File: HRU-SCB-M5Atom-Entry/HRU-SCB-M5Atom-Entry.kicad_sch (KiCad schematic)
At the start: 11 parts, among them J1 GROVE-CONNECTOR-DIP_4P-2.0_

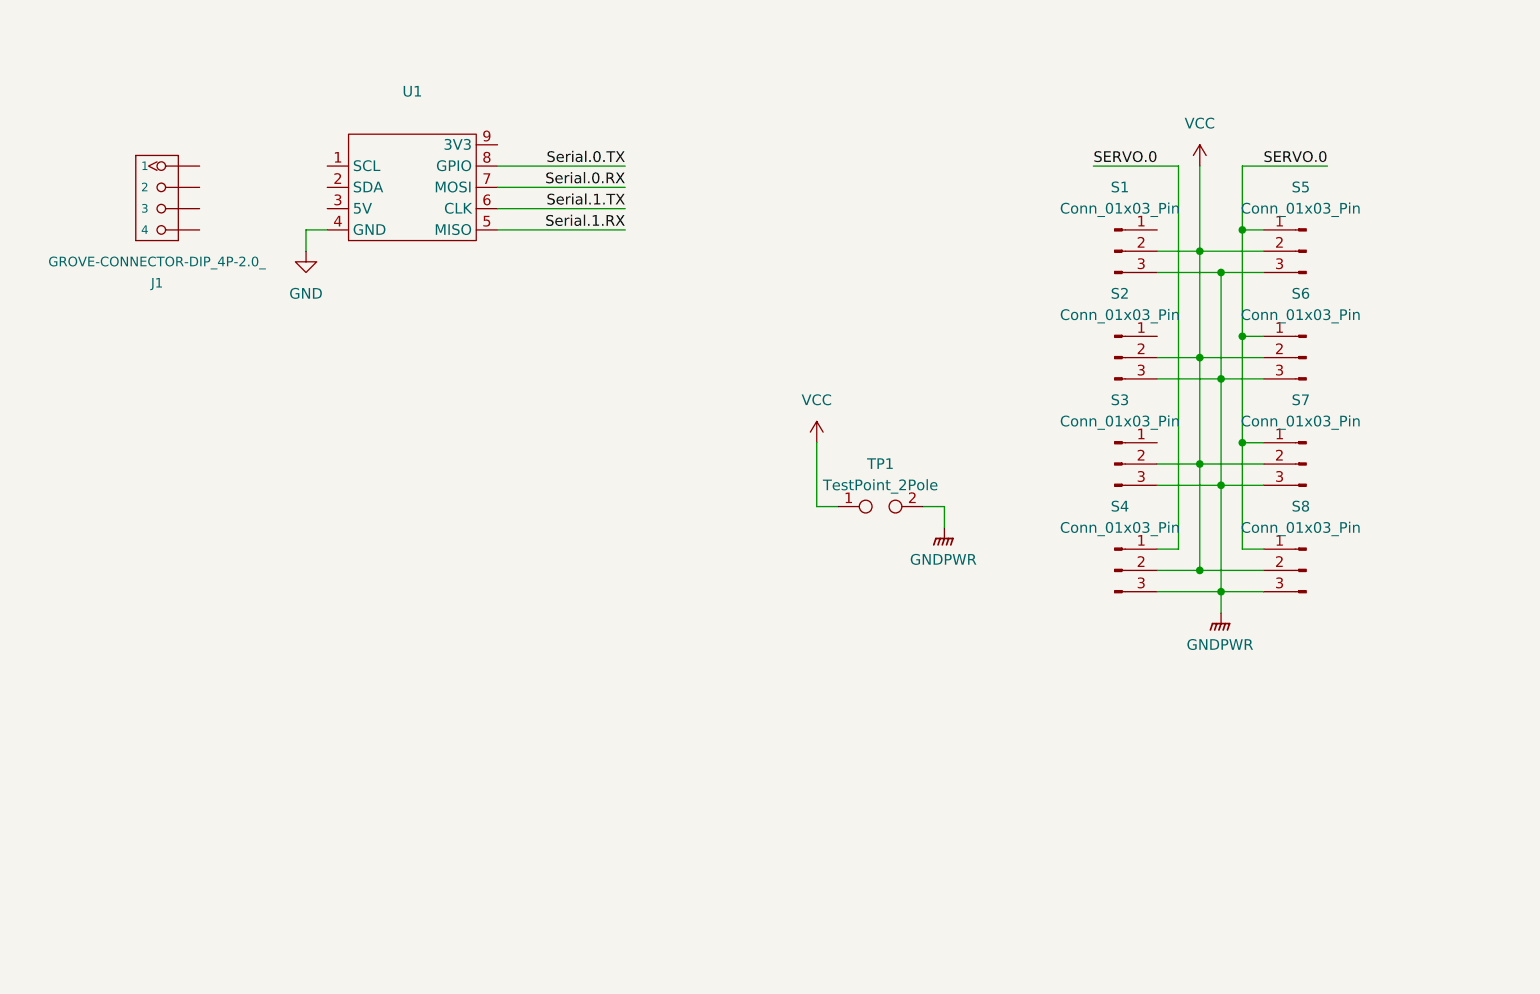
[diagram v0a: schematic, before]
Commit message: Update: M5Atom entry board with Grove port
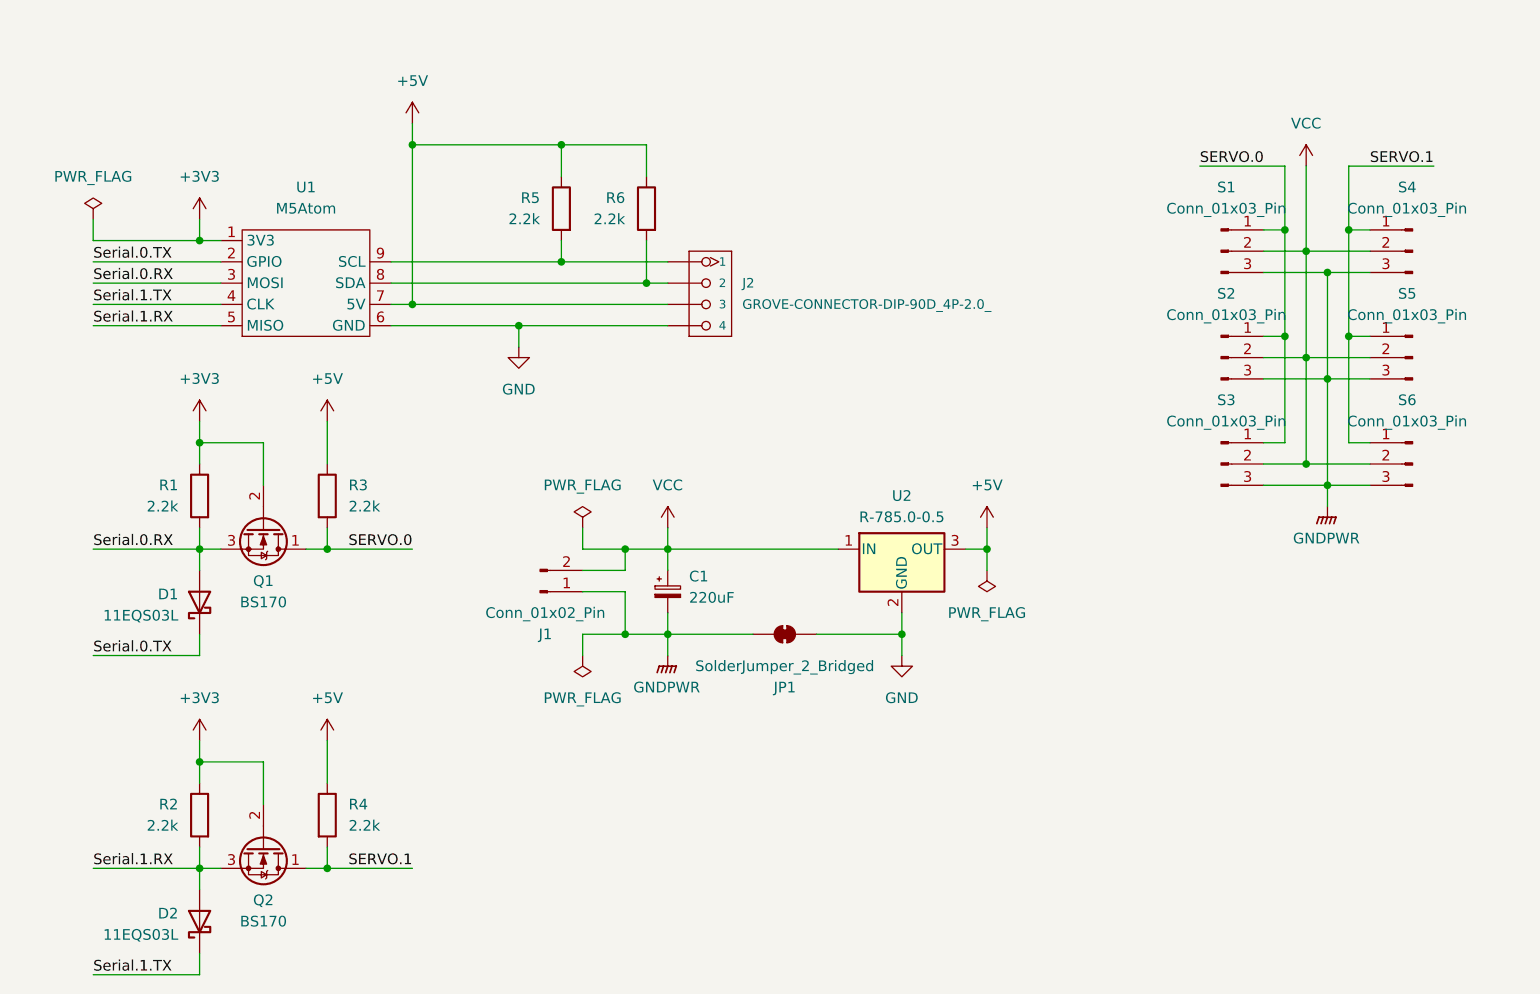
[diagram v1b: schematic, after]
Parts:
- removed J1: GROVE-CONNECTOR-DIP_4P-2.0_, OPL_Connector:GROVE-HW4-2.0, symbol OPL_Connector:GROVE-CONNECTOR-DIP_4P-2.0_
- removed S4, S7, S8: Conn_01x03_Pin, Connector_PinHeader_2.54mm:PinHeader_1x03_P2.54mm_Vertical, symbol Connector:Conn_01x03_Pin
- removed TP1: TestPoint_2Pole, TestPoint:TestPoint_2Pads_Pitch5.08mm_Drill1.3mm, symbol Connector:TestPoint_2Pole
- added C1: 220uF, Capacitor_THT:CP_Radial_D6.3mm_P2.50mm, symbol Device:C_Polarized_Small
- added D1, D2: 11EQS03L, Diode_THT:D_T-1_P5.08mm_Horizontal, symbol Device:D_Schottky
- added J1: Conn_01x02_Pin, Connector_AMASS:AMASS_XT30U-M_1x02_P5.0mm_Vertical, symbol Connector:Conn_01x02_Pin
- added J2: GROVE-CONNECTOR-DIP-90D_4P-2.0_, OPL_Connector:GROVE-HW4-2.0-90D, symbol OPL_Connector:GROVE-CONNECTOR-DIP-90D_4P-2.0_
- added JP1: SolderJumper_2_Bridged, Jumper:SolderJumper-2_P1.3mm_Bridged_Pad1.0x1.5mm, symbol Jumper:SolderJumper_2_Bridged
- added Q1, Q2: BS170, Package_TO_SOT_THT:TO-92_Inline, symbol Transistor_FET:BS170
- added R1, R2, R3, R4, R5, R6: 2.2k, Resistor_THT:R_Axial_DIN0207_L6.3mm_D2.5mm_P7.62mm_Horizontal, symbol Device:R
- added S6: Conn_01x03_Pin, Connector_PinHeader_2.54mm:PinHeader_1x03_P2.54mm_Vertical, symbol Connector:Conn_01x03_Pin
- added U2: R-785.0-0.5, Converter_DCDC:Converter_DCDC_RECOM_R-78E-0.5_THT, symbol Regulator_Switching:R-785.0-0.5
- U1: value ~ -> M5Atom
- renumbered S5 to S4, S6 to S5
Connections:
- net GND: now also U1.6 (GND), J2.4, JP1.2 (B), U2.2 (GND); no longer U1.4 (GND)
- net GNDPWR: now also C1.2, J1.1 (Pin_1), JP1.1 (A), S6.3 (Pin_3)
- net SERVO.0: now also S1.1 (Pin_1), S2.1 (Pin_1), S3.1 (Pin_1), Q1.1 (D), R3.2; no longer S4.1 (Pin_1), S5.1 (Pin_1)
- net Serial.0.RX: now also U1.3 (MOSI), D1.2 (A), Q1.3 (S), R1.2; no longer U1.7 (MOSI)
- net Serial.0.TX: now also U1.2 (GPIO), D1.1 (K); no longer U1.8 (GPIO)
- net Serial.1.RX: now also D2.2 (A), Q2.3 (S), R2.2
- net Serial.1.TX: now also U1.4 (CLK), D2.1 (K); no longer U1.6 (CLK)
- net VCC: now also C1.1, J1.2 (Pin_2), S6.2 (Pin_2), U2.1 (IN)
- net +3V3: now reaches U1.1 (3V3)
- net +3V3: now also Q1.2 (G), Q2.2 (G), R1.1, R2.1
- net at U1.9 (SCL): now also J2.1, R5.2
- new net: J2.2, R6.2, U1.8 (SDA)
- new net +5V: J2.3, R3.1, R4.1, R5.1, R6.1, U1.7 (5V), U2.3 (OUT)
- new net SERVO.1: Q2.1 (D), R4.2, S4.1 (Pin_1), S5.1 (Pin_1), S6.1 (Pin_1)
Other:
- moved on the sheet: S1, S2, S4, S5

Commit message: Update: parts layout and smaller board
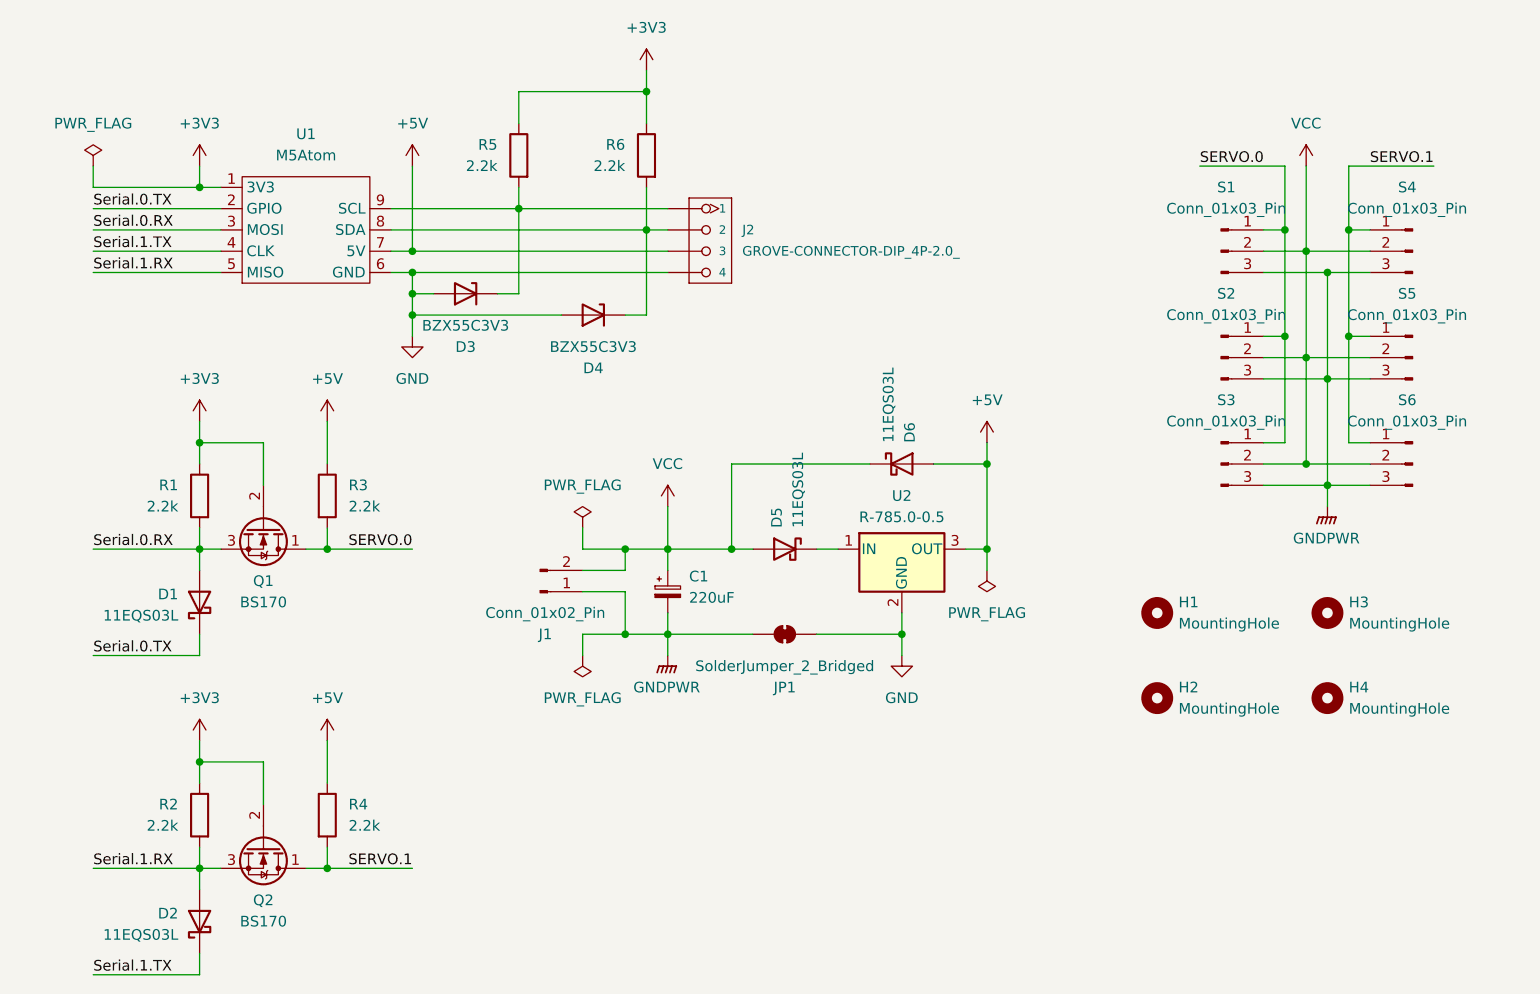
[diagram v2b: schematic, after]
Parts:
- removed J2: GROVE-CONNECTOR-DIP-90D_4P-2.0_, OPL_Connector:GROVE-HW4-2.0-90D, symbol OPL_Connector:GROVE-CONNECTOR-DIP-90D_4P-2.0_
- added D3, D4: BZX55C3V3, Diode_THT:D_T-1_P5.08mm_Horizontal, symbol Device:D_Zener
- added D5, D6: 11EQS03L, Diode_THT:D_T-1_P5.08mm_Horizontal, symbol Device:D_Schottky
- added H1, H2, H3, H4: MountingHole, MountingHole:MountingHole_2.2mm_M2, symbol Mechanical:MountingHole
- added J2: GROVE-CONNECTOR-DIP_4P-2.0_, OPL_Connector:GROVE-HW4-2.0, symbol OPL_Connector:GROVE-CONNECTOR-DIP_4P-2.0_
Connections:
- net +3V3: now also R5.1, R6.1
- net +5V: now also D6.2 (A), J2.3; no longer R5.1, R6.1
- net GND: now also D3.2 (A), D4.2 (A), J2.4
- net VCC: now also D5.2 (A), D6.1 (K); no longer U2.1 (IN)
- net at R6.2, U1.8 (SDA): now also D4.1 (K), J2.2
- net at R5.2, U1.9 (SCL): now also D3.1 (K), J2.1
- new net: D5.1 (K), U2.1 (IN)
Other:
- moved on the sheet: R5, R6, U1

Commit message: update: non-via circuit
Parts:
- S1, S2, S3, S4, S5, S6: footprint Connector_PinHeader_2.54mm:PinHeader_1x03_P2.54mm_Vertical -> mymod:PinHeader_1x03_P2.54mm_Vertical_SmallCourtyard
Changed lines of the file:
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@@
 			)
 		)
-		(property "Footprint" "Connector_PinHeader_2.54mm:PinHeader_1x03_P2.54mm_Vertical"
+		(property "Footprint" "mymod:PinHeader_1x03_P2.54mm_Vertical_SmallCourtyard"
 			(at 182.88 66.04 0)
 			(effects
@@
 			)
 		)
-		(property "Footprint" "Connector_PinHeader_2.54mm:PinHeader_1x03_P2.54mm_Vertical"
+		(property "Footprint" "mymod:PinHeader_1x03_P2.54mm_Vertical_SmallCourtyard"
 			(at 182.88 40.64 0)
 			(effects
@@
 			)
 		)
-		(property "Footprint" "Connector_PinHeader_2.54mm:PinHeader_1x03_P2.54mm_Vertical"
+		(property "Footprint" "mymod:PinHeader_1x03_P2.54mm_Vertical_SmallCourtyard"
 			(at 160.02 66.04 0)
 			(effects
@@
 			)
 		)
-		(property "Footprint" "Connector_PinHeader_2.54mm:PinHeader_1x03_P2.54mm_Vertical"
+		(property "Footprint" "mymod:PinHeader_1x03_P2.54mm_Vertical_SmallCourtyard"
 			(at 160.02 53.34 0)
 			(effects
@@
 			)
 		)
-		(property "Footprint" "Connector_PinHeader_2.54mm:PinHeader_1x03_P2.54mm_Vertical"
+		(property "Footprint" "mymod:PinHeader_1x03_P2.54mm_Vertical_SmallCourtyard"
 			(at 182.88 53.34 0)
 			(effects
@@
 			)
 		)
-		(property "Footprint" "Connector_PinHeader_2.54mm:PinHeader_1x03_P2.54mm_Vertical"
+		(property "Footprint" "mymod:PinHeader_1x03_P2.54mm_Vertical_SmallCourtyard"
 			(at 160.02 40.64 0)
 			(effects

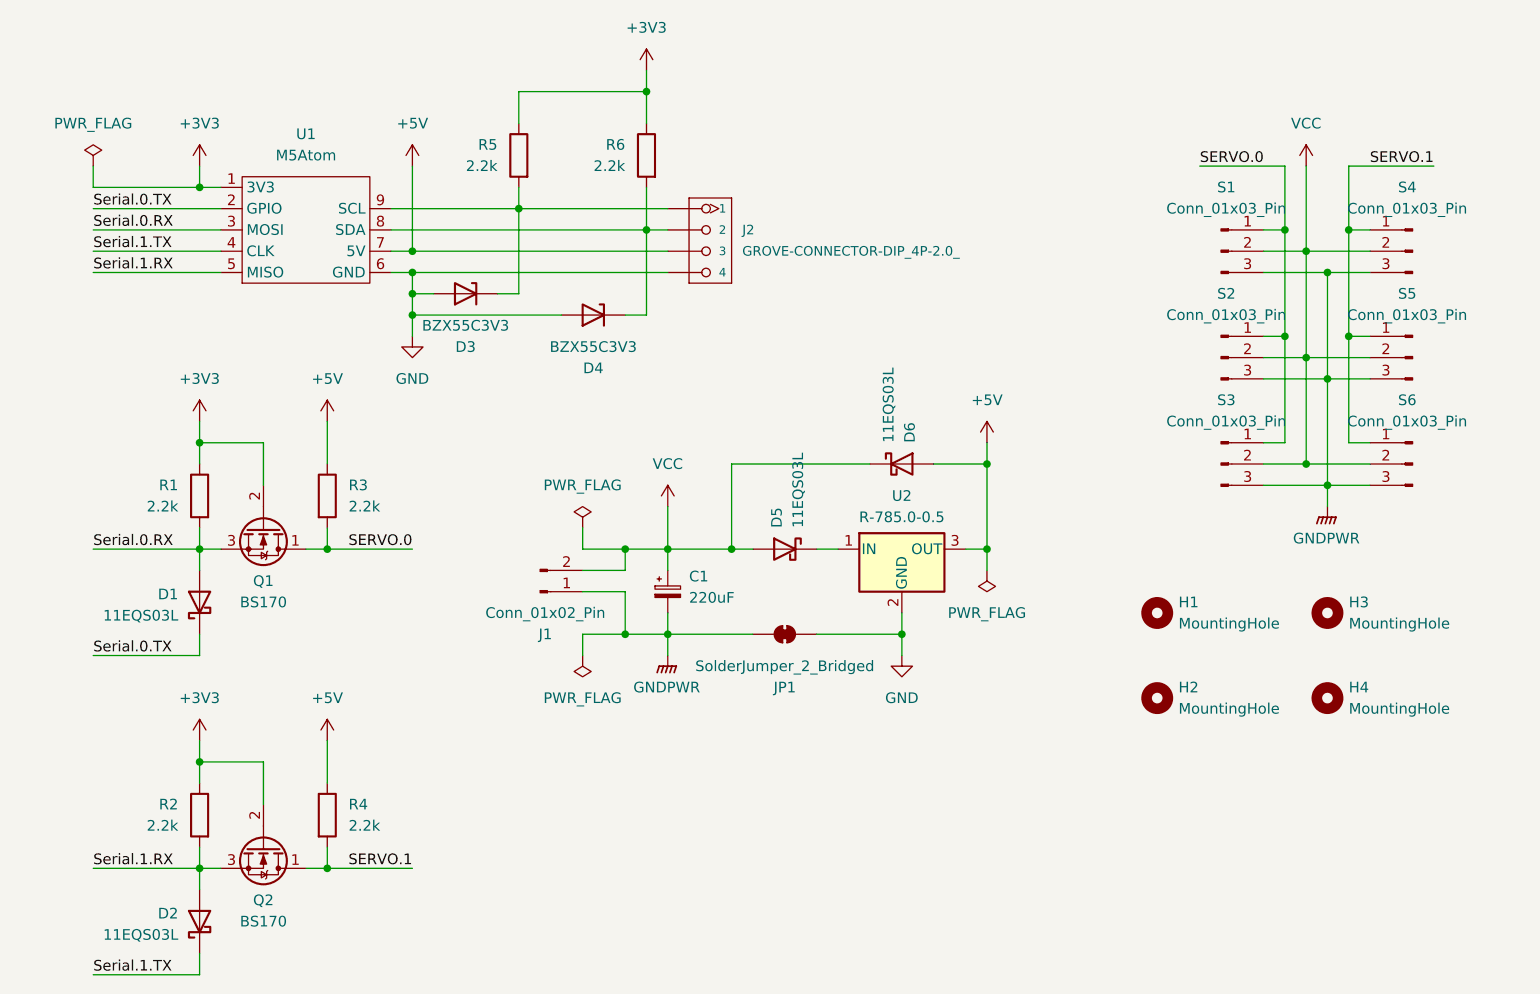
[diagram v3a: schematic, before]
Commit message: update: larger board outline for flesh members
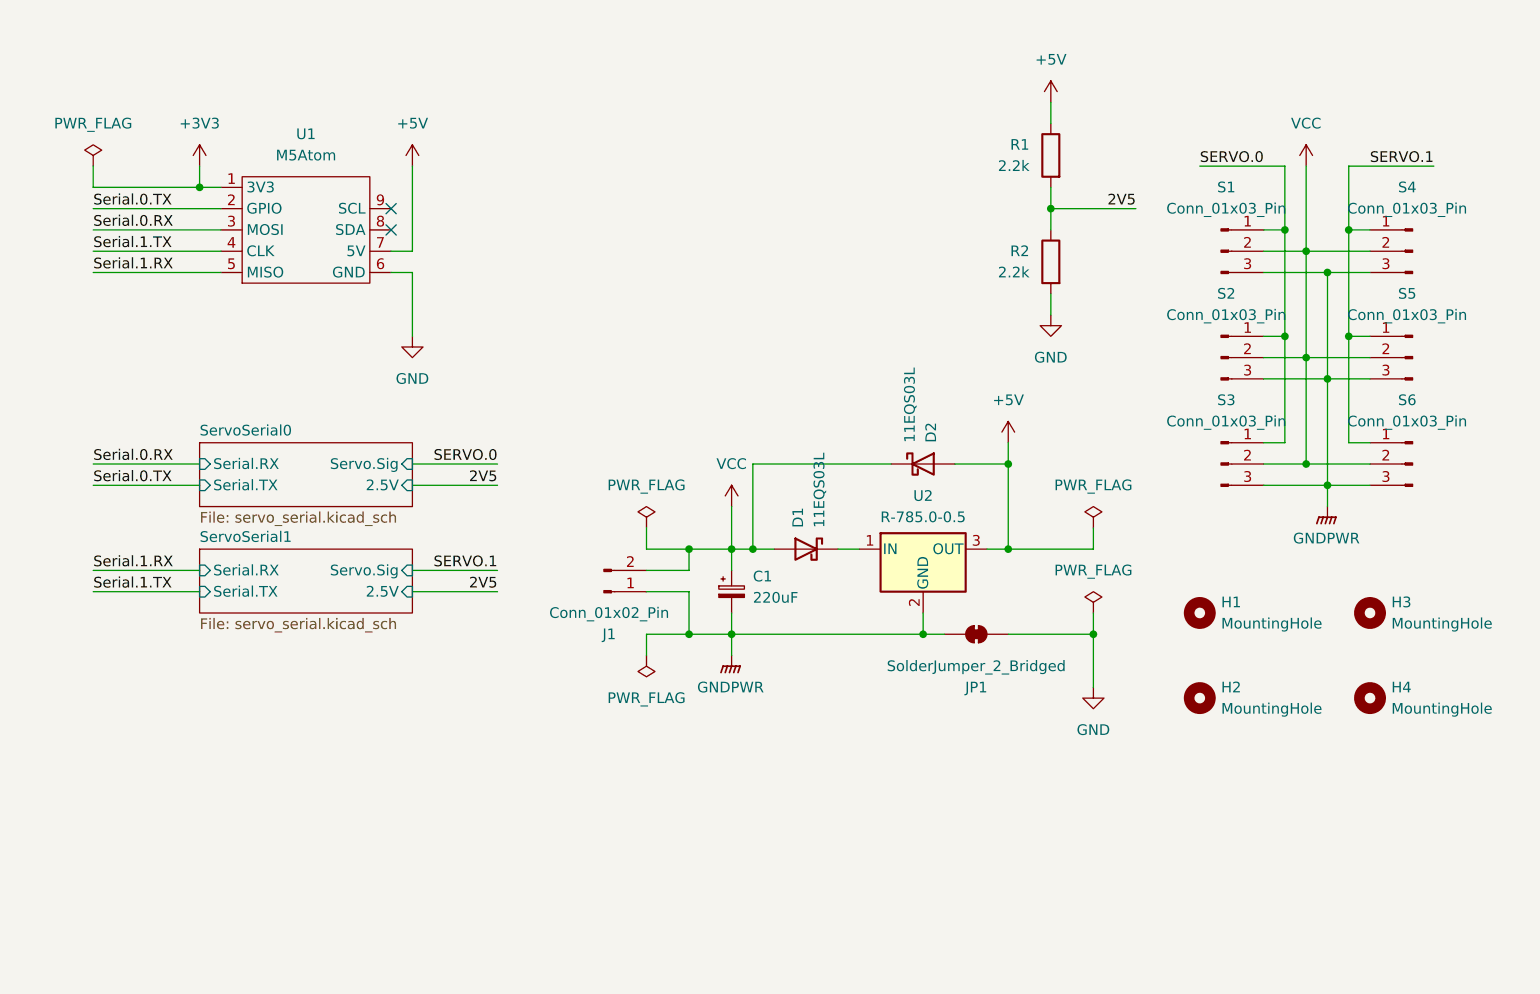
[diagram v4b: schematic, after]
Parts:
- removed D1, D2: 11EQS03L, Diode_THT:D_T-1_P5.08mm_Horizontal, symbol Device:D_Schottky
- removed D3, D4: BZX55C3V3, Diode_THT:D_T-1_P5.08mm_Horizontal, symbol Device:D_Zener
- removed J2: GROVE-CONNECTOR-DIP_4P-2.0_, OPL_Connector:GROVE-HW4-2.0, symbol OPL_Connector:GROVE-CONNECTOR-DIP_4P-2.0_
- removed Q1, Q2: BS170, Package_TO_SOT_THT:TO-92_Inline, symbol Transistor_FET:BS170
- removed R3, R4, R5, R6: 2.2k, Resistor_THT:R_Axial_DIN0207_L6.3mm_D2.5mm_P7.62mm_Horizontal, symbol Device:R
- renumbered D5 to D1, D6 to D2
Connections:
- net +3V3: no longer R1.1, R2.1
- net +5V: now also R1.1
- net GND: now also R2.2; no longer U2.2 (GND)
- net GNDPWR: now also U2.2 (GND)
- net Serial.0.RX: no longer R1.2
- net Serial.1.RX: no longer R2.2
- new net 2V5: R1.2, R2.1
- no-connect marks 0 -> 2
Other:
- added sheet ServoSerial0 (servo_serial.kicad_sch)
- added sheet ServoSerial1 (servo_serial.kicad_sch)
- moved on the sheet: C1, D1, D2, H1, H2, H3, H4, J1, JP1, U2

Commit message: Update: PCB wires
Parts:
- C1: AKI_CODE (none) -> 110272; AKI_URL (none) -> https://akizukidenshi.com/catalog/g/g110272/
- J1: AKI_CODE (none) -> 117951; AKI_URL (none) -> https://akizukidenshi.com/catalog/g/g117951/
- R1, R2: AKI_CODE (none) -> 125222; AKI_URL (none) -> https://akizukidenshi.com/catalog/g/g125222/
- S1, S2, S3, S4, S5, S6: AKI_CODE (none) -> 103949; AKI_URL (none) -> https://akizukidenshi.com/catalog/g/g103949/
- U1: AKI_CODE (none) -> 117209; AKI_URL (none) -> https://akizukidenshi.com/catalog/g/g117209/
- U2: AKI_CODE (none) -> 106353; AKI_URL (none) -> https://akizukidenshi.com/catalog/g/g106353/
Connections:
- net Serial.0.RX: now also U1.2 (GPIO); no longer U1.3 (MOSI)
- net Serial.0.TX: now also U1.3 (MOSI); no longer U1.2 (GPIO)
- net Serial.1.RX: now also U1.4 (CLK); no longer U1.5 (MISO)
- net Serial.1.TX: now also U1.5 (MISO); no longer U1.4 (CLK)
